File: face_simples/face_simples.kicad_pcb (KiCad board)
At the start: 2 copper layers, 147.5 x 115 mm, 12 parts

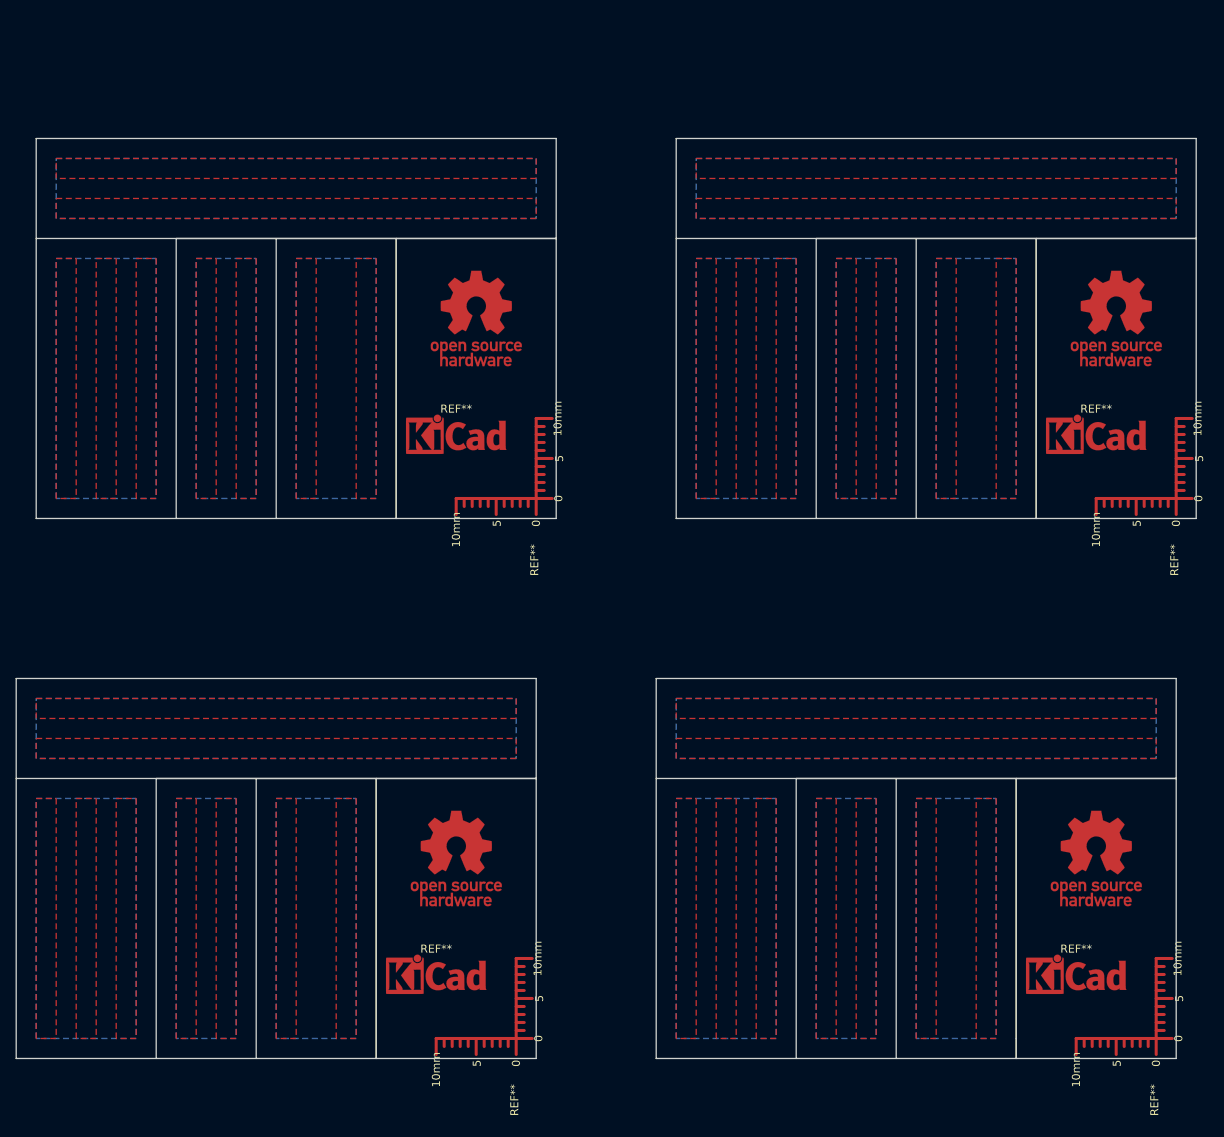
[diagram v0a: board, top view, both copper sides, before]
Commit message: Placa com trilha de formato ondulatório adicionada
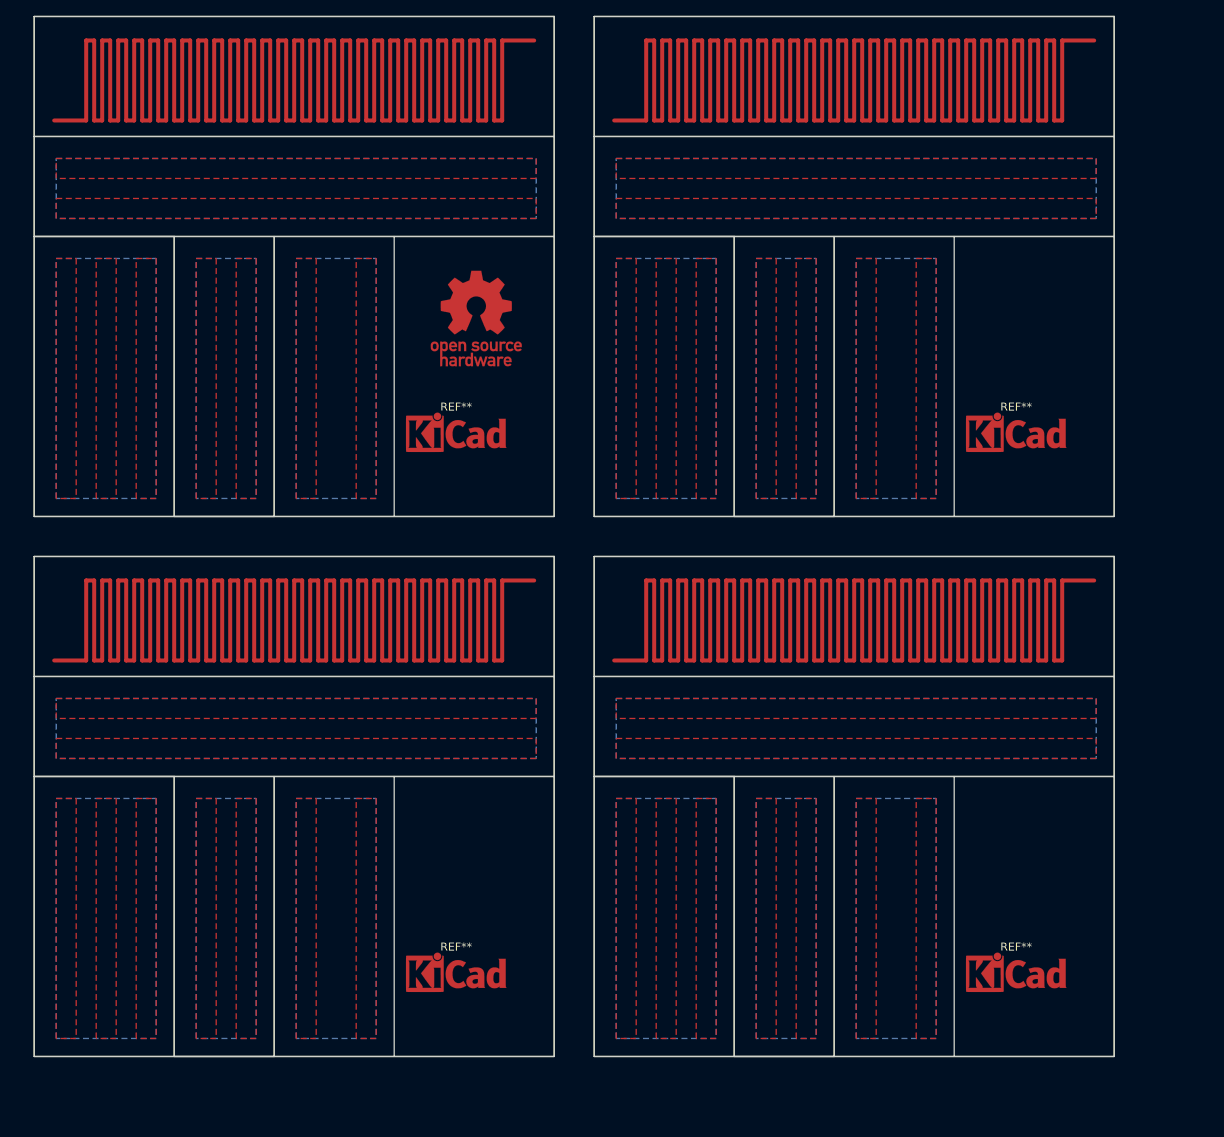
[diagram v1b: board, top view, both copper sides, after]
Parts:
- removed the REF** at (222.5, 152.5)
- removed the REF** at (145.0, 85.0)
- removed the REF** at (132.5, 145.0)
- removed the REF** at (135.0, 130.0)
- removed the REF** at (142.5, 152.5)
- removed the REF** at (215.0, 130.0)
- removed the REF** at (212.5, 145.0)
- removed the REF** at (215.0, 77.5)
- removed the REF** at (217.5, 62.5)
- removed the REF** at (225.0, 85.0)
- added REF**: KiCad-Logo_5mm_Copper, Symbol:KiCad-Logo_5mm_Copper, F.Cu at (205.0, 144.8)
- added REF**: KiCad-Logo_5mm_Copper, Symbol:KiCad-Logo_5mm_Copper, F.Cu at (135.0, 144.8)
- added REF**: KiCad-Logo_5mm_Copper, Symbol:KiCad-Logo_5mm_Copper, F.Cu at (205.0, 77.2)
- moved REF** 0.25 mm to (135.0, 77.2)
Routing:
- net (no net): track 0.00 -> 2360.0 mm
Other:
- board size 147.5 x 115 mm -> 135 x 130 mm
- net class Default: clearance 0.2 -> 0.25; trace_width 0.25 -> 0.5
- rule trace_clearance: 0.2 -> 0.25

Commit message: PCB updated, last version.
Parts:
- added REF**: OSHW-Logo_11.4x12mm_Copper, Symbol:OSHW-Logo_11.4x12mm_Copper, F.Cu at (137.5, 130.0)
- added REF**: OSHW-Logo_11.4x12mm_Copper, Symbol:OSHW-Logo_11.4x12mm_Copper, F.Cu at (207.5, 130.0)
- added REF**: OSHW-Logo_11.4x12mm_Copper, Symbol:OSHW-Logo_11.4x12mm_Copper, F.Cu at (207.5, 62.5)

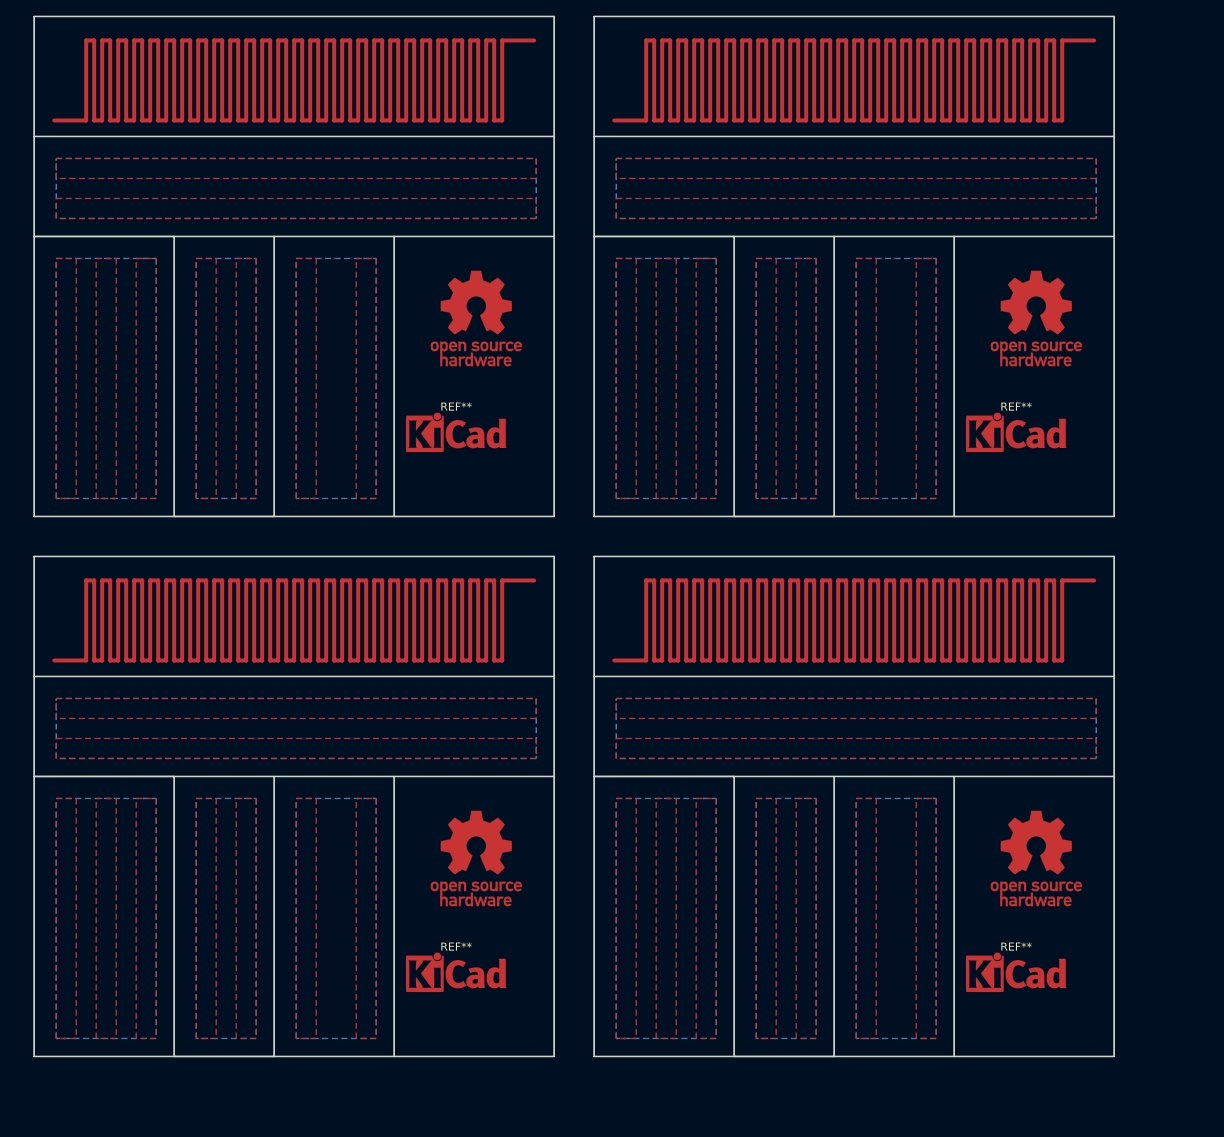
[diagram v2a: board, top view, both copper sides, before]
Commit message: Antena de 10cm adicionada
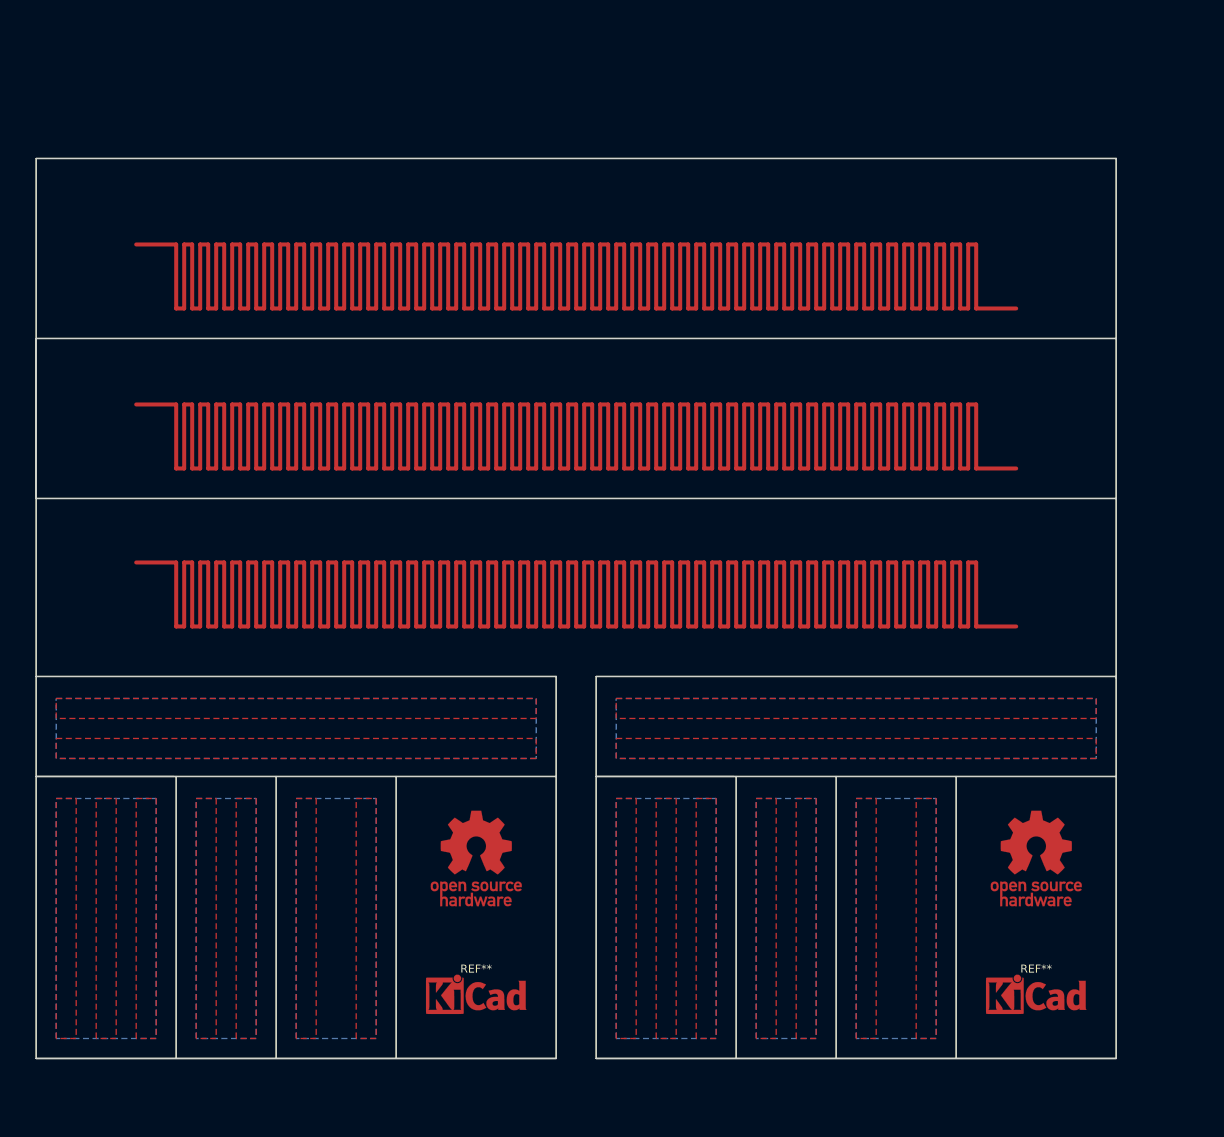
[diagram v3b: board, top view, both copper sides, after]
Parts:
- removed the REF** at (137.5, 130.0)
- removed the REF** at (207.5, 62.5)
- removed the REF** at (205.0, 144.8)
- removed the REF** at (135.0, 144.8)
- removed the REF** at (205.0, 77.2)
- removed the REF** at (135.0, 77.2)
- added REF**: KiCad-Logo_5mm_Copper, Symbol:KiCad-Logo_5mm_Copper, F.Cu at (207.5, 147.5)
- added REF**: KiCad-Logo_5mm_Copper, Symbol:KiCad-Logo_5mm_Copper, F.Cu at (137.5, 147.5)
- moved REF** 67.5 mm to (137.5, 130.0)
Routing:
- net (no net): track 2360.0 -> 2754.0 mm
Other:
- board size 135 x 130 mm -> 135 x 112.5 mm
